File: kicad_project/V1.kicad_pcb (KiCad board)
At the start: 2 copper layers, 17.8 x 52.1 mm, 16 parts, among them P1 CONN_02X03, Q1 FDN339AN, Q2 FDN339AN, U1 ATTINY85-S

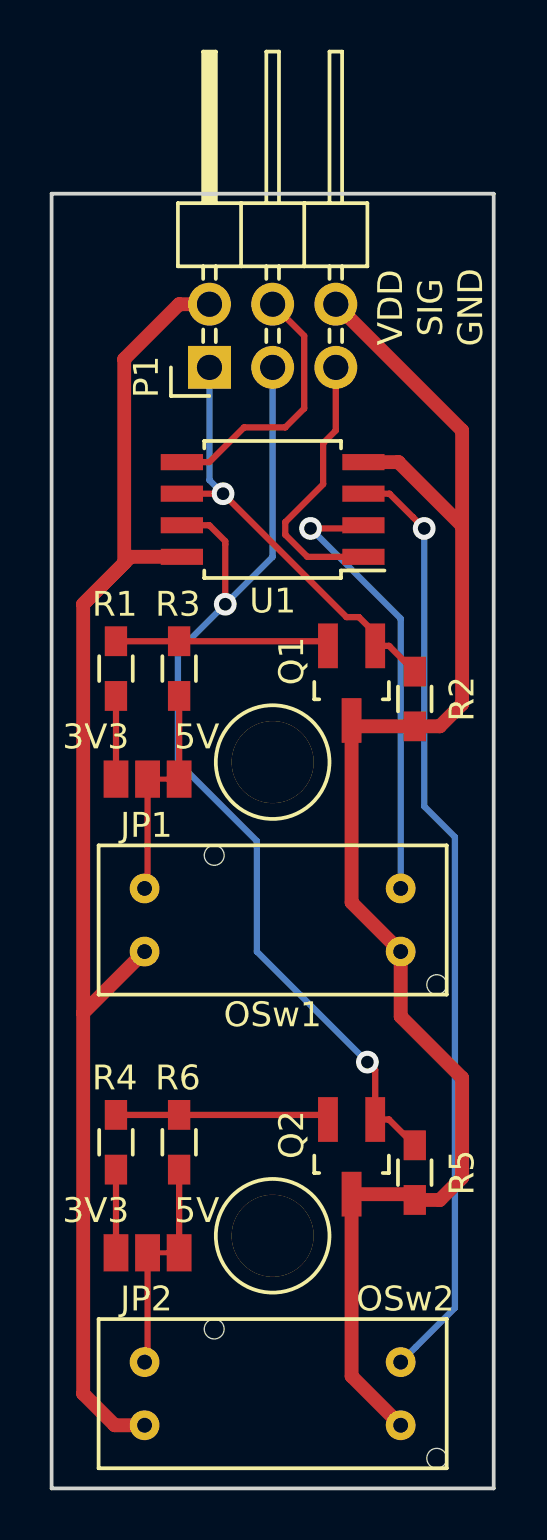
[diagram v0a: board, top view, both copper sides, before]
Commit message: Added dimentions to board
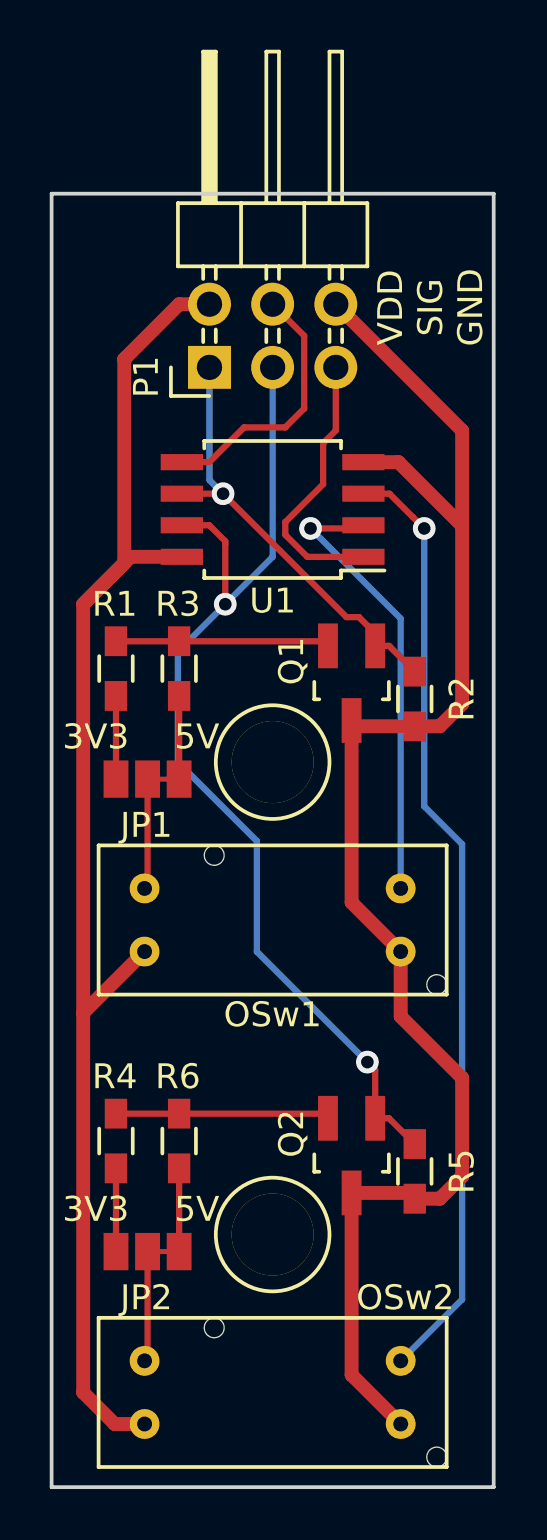
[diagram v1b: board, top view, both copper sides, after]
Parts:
- OSw1, OSw2: value Optical-interrupt-sensor -> ITR9606
- moved OSw2 0.05 mm to (114.3, 140.9)
- moved R5 0.05 mm to (120.0, 132.0)
- moved REF** 0.05 mm to (114.3, 134.6)
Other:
- board size 17.8 x 52.1 mm -> 17.8 x 52 mm
- board text added: "Ø 3.3mm"
